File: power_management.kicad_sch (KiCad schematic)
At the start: 23 parts, among them J1 705510001, Q1 SSM3J327R, U6 TPS22917DBV, U7 OPA333 or TLV333 or TLV9041

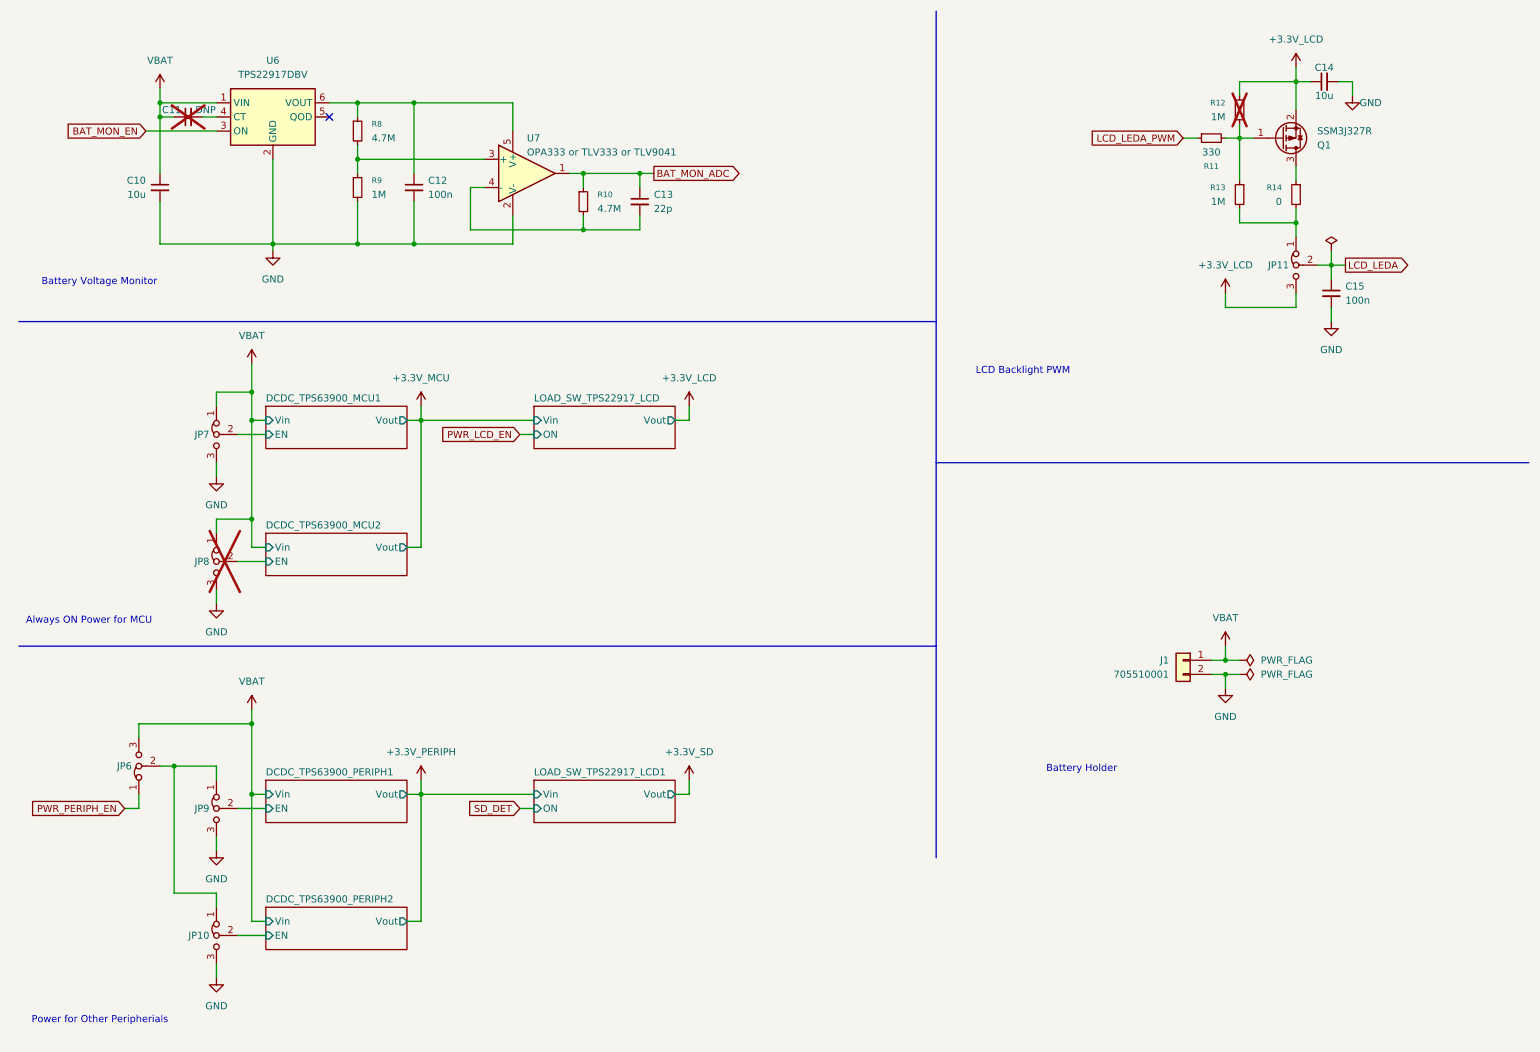
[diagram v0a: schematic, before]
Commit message: Initial layout before routing.
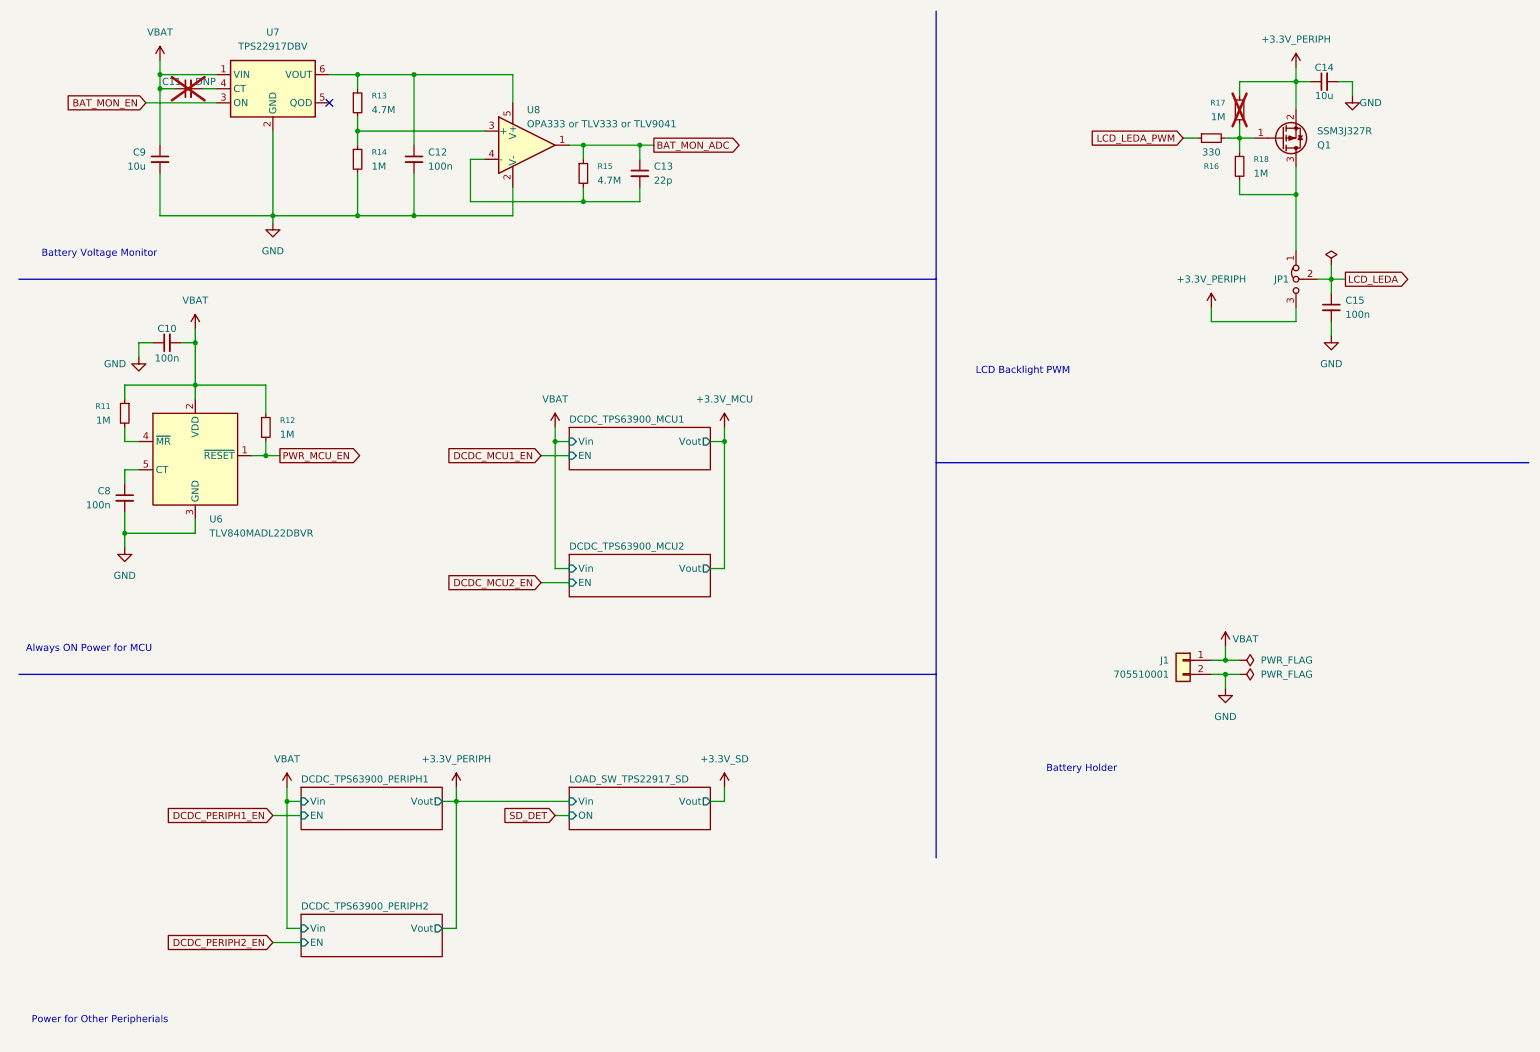
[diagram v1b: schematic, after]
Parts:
- removed JP10, JP6, JP7, JP8, JP9: Jumper_3_Bridged12, Connector_PinHeader_2.54mm:PinHeader_1x03_P2.54mm_Vertical, symbol Jumper:Jumper_3_Bridged12
- removed R14: 0, Resistor_SMD:R_0603_1608Metric_Pad0.98x0.95mm_HandSolder, symbol Device:R_Small
- added C10, C8: 100n, Capacitor_SMD:C_0603_1608Metric_Pad1.08x0.95mm_HandSolder, symbol Device:C_Small
- added R11, R12: 1M, Resistor_SMD:R_0603_1608Metric_Pad0.98x0.95mm_HandSolder, symbol Device:R_Small
- added U6: TLV840MADL22DBVR, Package_TO_SOT_SMD:SOT-23-5, symbol project_symbols:TLV840
- renumbered C10 to C9, JP11 to JP1, R8 to R13, R9 to R14, R10 to R15, R11 to R16, R12 to R17, R13 to R18, U6 to U7, U7 to U8
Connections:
- net +3.3V_LCD is gone; now on net +3.3V_PERIPH: C14.1, JP1.3 (B), Q1.2 (S), R17.1
- net GND: now also C10.1, C8.2, U6.3 (GND)
- net VBAT: now also C10.2, R11.1, R12.1, U6.2 (VDD)
- net at Q1.3 (D): now also JP1.1 (A), R18.2
- new net: R11.2, U6.4 (~{MR})
- new net: C8.1, U6.5 (CT)
- new net PWR_MCU_EN: R12.2, U6.1 (~{RESET})
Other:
- sheet LOAD_SW_TPS22917_LCD1 renamed LOAD_SW_TPS22917_SD
- removed sheet LOAD_SW_TPS22917_LCD
- moved on the sheet: C11, C12, C13, C15, C9, JP1, R13, R14, R15, R18, U7, U8

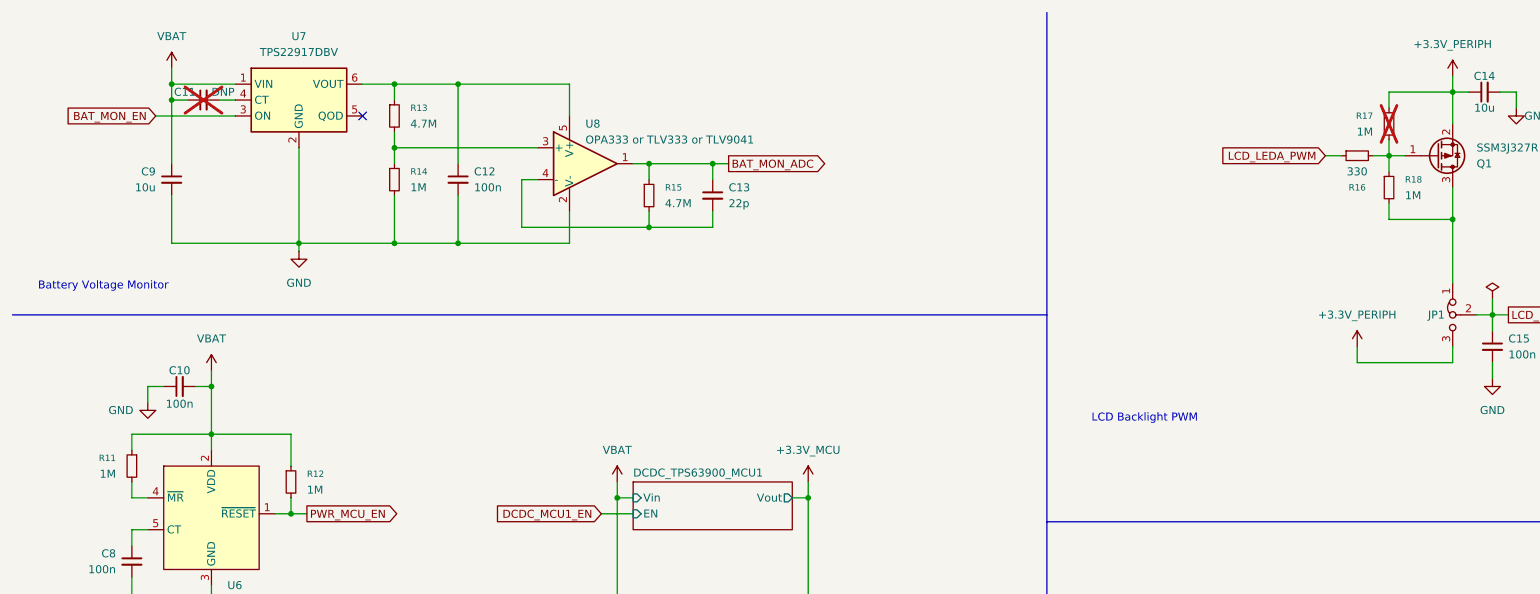
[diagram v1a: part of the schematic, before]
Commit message: PCB layout done, signal routing finished, power routing remaining.
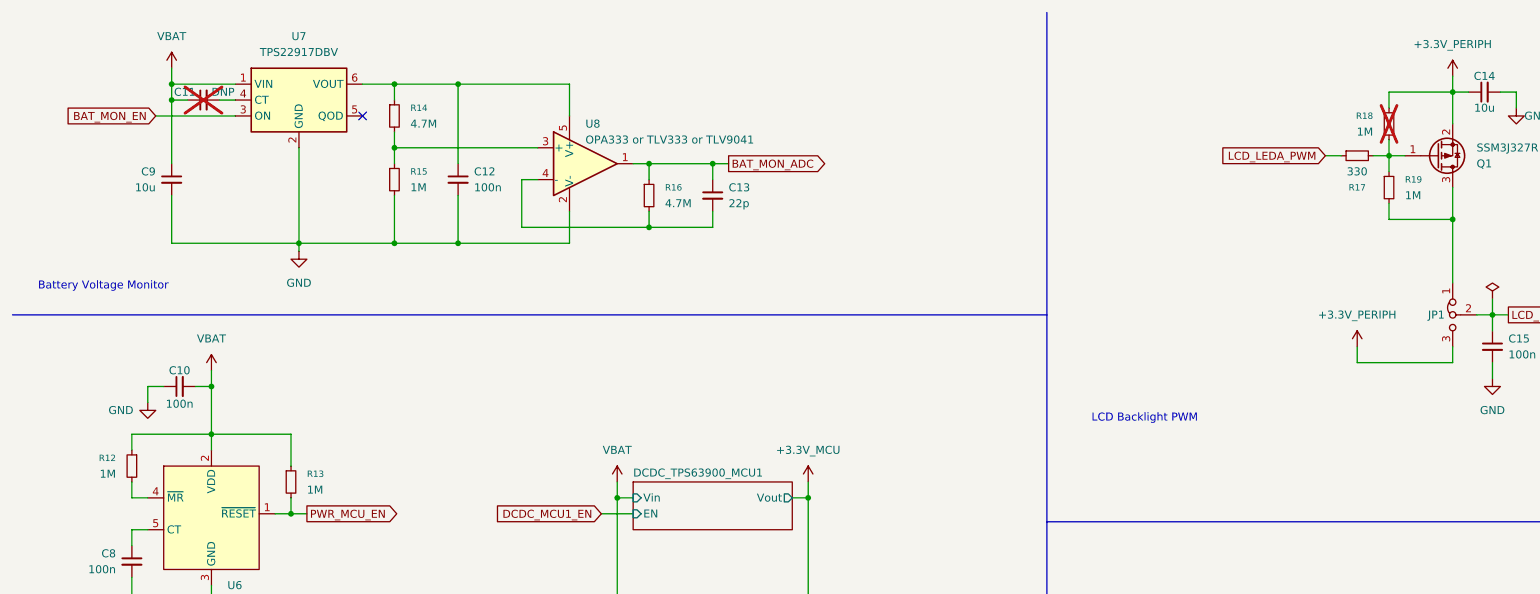
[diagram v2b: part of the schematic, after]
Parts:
- renumbered R11 to R12, R12 to R13, R13 to R14, R14 to R15, R15 to R16, R16 to R17, R17 to R18, R18 to R19
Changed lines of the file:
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@@
 		(dnp no)
 		(fields_autoplaced yes)
-		(property "Reference" "#PWR025"
+		(property "Reference" "#PWR026"
 			(at 60.96 156.21 0)
 			(hide yes)
@@
 			(project "DigiFur-Rev1.0"
 				(path "/47dbac06-588f-419b-91d0-b3790df884b4"
-					(reference "#PWR025")
+					(reference "#PWR026")
 					(unit 1)
 				)
@@
 		(in_pos_files yes)
 		(dnp no)
-		(property "Reference" "#PWR031"
+		(property "Reference" "#PWR032"
 			(at 229.87 130.81 0)
 			(hide yes)
@@
 			(project "DigiFur-Rev1.0"
 				(path "/47dbac06-588f-419b-91d0-b3790df884b4"
-					(reference "#PWR031")
+					(reference "#PWR032")
 					(unit 1)
 				)
@@
 		(dnp no)
 		(fields_autoplaced yes)
-		(property "Reference" "#PWR032"
+		(property "Reference" "#PWR033"
 			(at 229.87 140.97 0)
 			(hide yes)
@@
 			(project "DigiFur-Rev1.0"
 				(path "/47dbac06-588f-419b-91d0-b3790df884b4"
-					(reference "#PWR032")
+					(reference "#PWR033")
 					(unit 1)
 				)
@@
 		(in_pos_files yes)
 		(dnp no)
-		(property "Reference" "R16"
+		(property "Reference" "R17"
 			(at 227.33 40.64 90)
 			(show_name no)
@@
 			(project "DigiFur-Rev1.0"
 				(path "/47dbac06-588f-419b-91d0-b3790df884b4"
-					(reference "R16")
+					(reference "R17")
 					(unit 1)
 				)
@@
 		(dnp no)
 		(fields_autoplaced yes)
-		(property "Reference" "R15"
+		(property "Reference" "R16"
 			(at 116.84 40.6399 0)
 			(show_name no)
@@
 			(project "DigiFur-Rev1.0"
 				(path "/47dbac06-588f-419b-91d0-b3790df884b4"
-					(reference "R15")
+					(reference "R16")
 					(unit 1)
 				)
@@
 		(in_pos_files yes)
 		(dnp no)
-		(property "Reference" "#PWR035"
+		(property "Reference" "#PWR036"
 			(at 252.73 34.29 0)
 			(hide yes)
@@
 			(project "DigiFur-Rev1.0"
 				(path "/47dbac06-588f-419b-91d0-b3790df884b4"
-					(reference "#PWR035")
+					(reference "#PWR036")
 					(unit 1)
 				)
@@
 		(dnp no)
 		(fields_autoplaced yes)
-		(property "Reference" "#PWR024"
+		(property "Reference" "#PWR025"
 			(at 58.42 57.15 0)
 			(hide yes)
@@
 			(project "DigiFur-Rev1.0"
 				(path "/47dbac06-588f-419b-91d0-b3790df884b4"
-					(reference "#PWR024")
+					(reference "#PWR025")
 					(unit 1)
 				)
@@
 		(dnp no)
 		(fields_autoplaced yes)
-		(property "Reference" "#PWR026"
+		(property "Reference" "#PWR027"
 			(at 91.44 156.21 0)
 			(hide yes)
@@
 			(project "DigiFur-Rev1.0"
 				(path "/47dbac06-588f-419b-91d0-b3790df884b4"
-					(reference "#PWR026")
+					(reference "#PWR027")
 					(unit 1)
 				)
@@
 		(dnp no)
 		(fields_autoplaced yes)
-		(property "Reference" "#PWR028"
+		(property "Reference" "#PWR029"
 			(at 139.7 91.44 0)
 			(hide yes)
@@
 			(project "DigiFur-Rev1.0"
 				(path "/47dbac06-588f-419b-91d0-b3790df884b4"
-					(reference "#PWR028")
+					(reference "#PWR029")
 					(unit 1)
 				)
@@
 		(in_pos_files yes)
 		(dnp no)
-		(property "Reference" "R11"
+		(property "Reference" "R12"
 			(at 29.21 83.8199 0)
 			(show_name no)
@@
 			(project "DigiFur-Rev1.0"
 				(path "/47dbac06-588f-419b-91d0-b3790df884b4"
-					(reference "R11")
+					(reference "R12")
 					(unit 1)
 				)
@@
 		(dnp no)
 		(fields_autoplaced yes)
-		(property "Reference" "R14"
+		(property "Reference" "R15"
 			(at 76.2 38.0999 0)
 			(show_name no)
@@
 			(project "DigiFur-Rev1.0"
 				(path "/47dbac06-588f-419b-91d0-b3790df884b4"
-					(reference "R14")
+					(reference "R15")
 					(unit 1)
 				)
@@
 		(dnp no)
 		(fields_autoplaced yes)
-		(property "Reference" "#PWR020"
+		(property "Reference" "#PWR021"
 			(at 31.75 115.57 0)
 			(hide yes)
@@
 			(project "DigiFur-Rev1.0"
 				(path "/47dbac06-588f-419b-91d0-b3790df884b4"
-					(reference "#PWR020")
+					(reference "#PWR021")
 					(unit 1)
 				)
@@
 		(dnp no)
 		(fields_autoplaced yes)
-		(property "Reference" "#PWR034"
+		(property "Reference" "#PWR035"
 			(at 248.92 77.47 0)
 			(hide yes)
@@
 			(project "DigiFur-Rev1.0"
 				(path "/47dbac06-588f-419b-91d0-b3790df884b4"
-					(reference "#PWR034")
+					(reference "#PWR035")
 					(unit 1)
 				)
@@
 		(dnp no)
 		(fields_autoplaced yes)
-		(property "Reference" "#PWR022"
+		(property "Reference" "#PWR023"
 			(at 38.1 25.4 0)
 			(hide yes)
@@
 			(project "DigiFur-Rev1.0"
 				(path "/47dbac06-588f-419b-91d0-b3790df884b4"
-					(reference "#PWR022")
+					(reference "#PWR023")
 					(unit 1)
 				)
@@
 		(in_pos_files yes)
 		(dnp no)
-		(property "Reference" "#PWR021"
+		(property "Reference" "#PWR022"
 			(at 34.29 81.28 0)
 			(hide yes)
@@
 			(project "DigiFur-Rev1.0"
 				(path "/47dbac06-588f-419b-91d0-b3790df884b4"
-					(reference "#PWR021")
+					(reference "#PWR022")
 					(unit 1)
 				)
@@
 		(dnp no)
 		(fields_autoplaced yes)
-		(property "Reference" "#PWR033"
+		(property "Reference" "#PWR034"
 			(at 242.57 26.67 0)
 			(hide yes)
@@
 			(project "DigiFur-Rev1.0"
 				(path "/47dbac06-588f-419b-91d0-b3790df884b4"
-					(reference "#PWR033")
+					(reference "#PWR034")
 					(unit 1)
 				)
@@
 		(dnp no)
 		(fields_autoplaced yes)
-		(property "Reference" "#PWR030"
+		(property "Reference" "#PWR031"
 			(at 227.33 69.85 0)
 			(hide yes)
@@
 			(project "DigiFur-Rev1.0"
 				(path "/47dbac06-588f-419b-91d0-b3790df884b4"
-					(reference "#PWR030")
+					(reference "#PWR031")
 					(unit 1)
 				)
@@
 		(dnp no)
 		(fields_autoplaced yes)
-		(property "Reference" "#PWR029"
+		(property "Reference" "#PWR030"
 			(at 139.7 156.21 0)
 			(hide yes)
@@
 			(project "DigiFur-Rev1.0"
 				(path "/47dbac06-588f-419b-91d0-b3790df884b4"
-					(reference "#PWR029")
+					(reference "#PWR030")
 					(unit 1)
 				)
@@
 		(dnp no)
 		(fields_autoplaced yes)
-		(property "Reference" "R13"
+		(property "Reference" "R14"
 			(at 76.2 27.9399 0)
 			(show_name no)
@@
 			(project "DigiFur-Rev1.0"
 				(path "/47dbac06-588f-419b-91d0-b3790df884b4"
-					(reference "R13")
+					(reference "R14")
 					(unit 1)
 				)
@@
 		(in_pos_files yes)
 		(dnp no)
-		(property "Reference" "R18"
+		(property "Reference" "R19"
 			(at 234.95 39.3699 0)
 			(show_name no)
@@
 			(project "DigiFur-Rev1.0"
 				(path "/47dbac06-588f-419b-91d0-b3790df884b4"
-					(reference "R18")
+					(reference "R19")
 					(unit 1)
 				)
@@
 		(dnp no)
 		(fields_autoplaced yes)
-		(property "Reference" "#PWR027"
+		(property "Reference" "#PWR028"
 			(at 109.22 91.44 0)
 			(hide yes)
@@
 			(project "DigiFur-Rev1.0"
 				(path "/47dbac06-588f-419b-91d0-b3790df884b4"
-					(reference "#PWR027")
+					(reference "#PWR028")
 					(unit 1)
 				)
@@
 		(dnp no)
 		(fields_autoplaced yes)
-		(property "Reference" "R12"
+		(property "Reference" "R13"
 			(at 59.69 86.3599 0)
 			(show_name no)
@@
 			(project "DigiFur-Rev1.0"
 				(path "/47dbac06-588f-419b-91d0-b3790df884b4"
-					(reference "R12")
+					(reference "R13")
 					(unit 1)
 				)
@@
 		(in_pos_files yes)
 		(dnp yes)
-		(property "Reference" "R17"
+		(property "Reference" "R18"
 			(at 229.87 29.2099 0)
 			(show_name no)
@@
 			(project "DigiFur-Rev1.0"
 				(path "/47dbac06-588f-419b-91d0-b3790df884b4"
-					(reference "R17")
+					(reference "R18")
 					(unit 1)
 				)
@@
 		(dnp no)
 		(fields_autoplaced yes)
-		(property "Reference" "#PWR023"
+		(property "Reference" "#PWR024"
 			(at 44.45 73.66 0)
 			(hide yes)
@@
 			(project "DigiFur-Rev1.0"
 				(path "/47dbac06-588f-419b-91d0-b3790df884b4"
-					(reference "#PWR023")
+					(reference "#PWR024")
 					(unit 1)
 				)
